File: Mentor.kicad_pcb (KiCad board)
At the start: 2 copper layers, 50 x 100 mm, 41 parts, among them J1 CONN_01X02, J2 CONN_01X06, J3 CONN_01X09, J4 CONN_01X10, J5 CONN_01X02, J6 CONN_01X03, J7 CONN_01X09, Q1 PZT2222A, Q2 PZT2222A, Q3 IRFR3303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

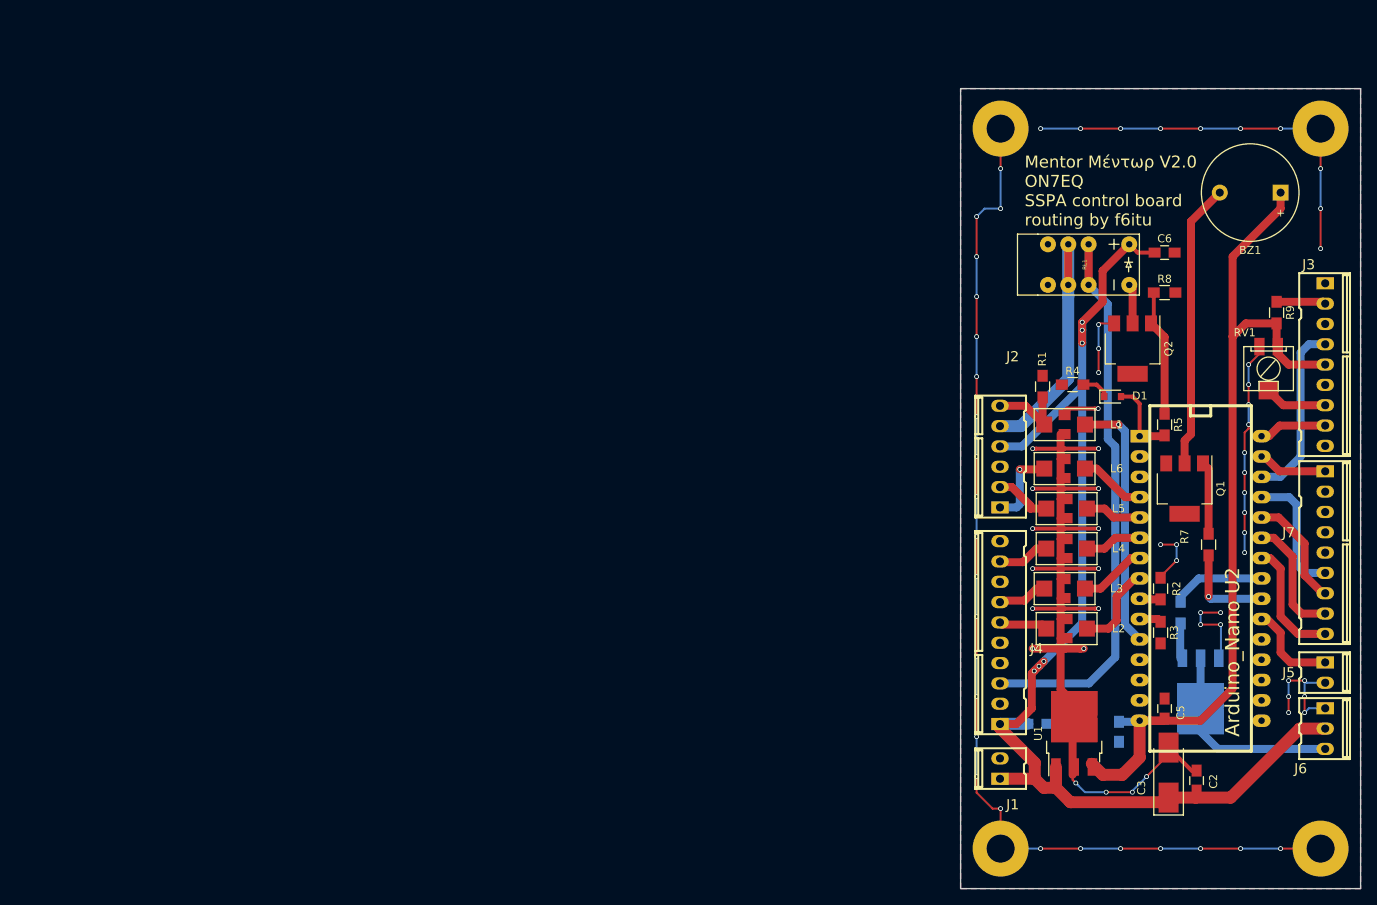
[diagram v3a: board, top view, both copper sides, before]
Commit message: Mentor V3.0 W6PQL compatible
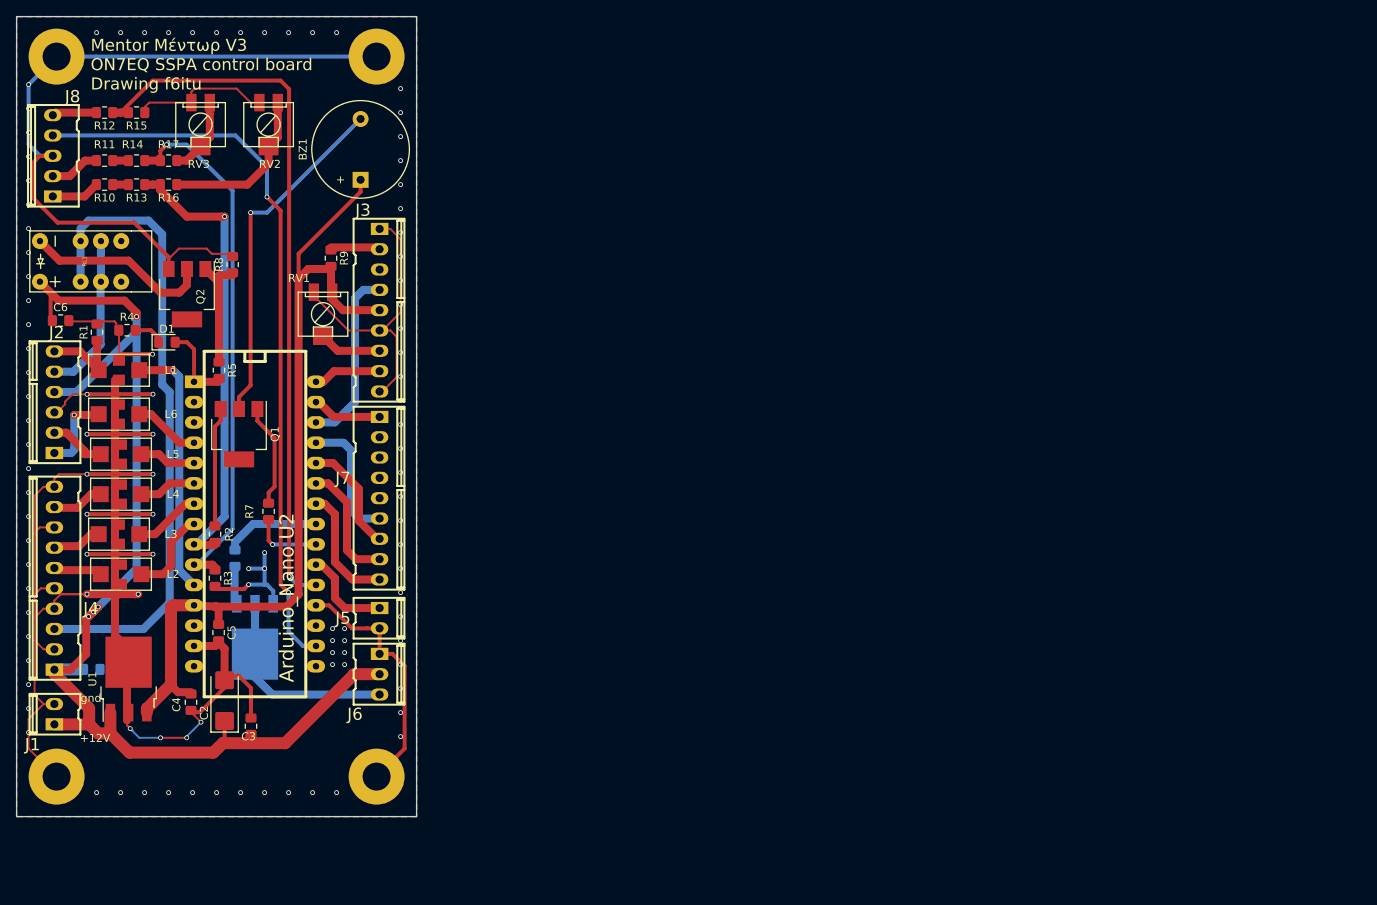
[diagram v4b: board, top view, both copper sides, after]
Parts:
- added J8: Conn_01x05, conn_kk100:kk100_22-23-2051, F.Cu at (46.6, 43.4)
- added R10: 5k, Resistor_SMD:R_0805_2012Metric_Pad1.15x1.40mm_HandSolder, F.Cu at (53.0, 47.0)
- added R11: 1k5, Resistor_SMD:R_0805_2012Metric_Pad1.15x1.40mm_HandSolder, F.Cu at (53.0, 44.0)
- added R12: 3k3, Resistor_SMD:R_0805_2012Metric_Pad1.15x1.40mm_HandSolder, F.Cu at (53.0, 38.0)
- added R13: 2k, Resistor_SMD:R_0805_2012Metric_Pad1.15x1.40mm_HandSolder, F.Cu at (57.0, 47.0)
- added R14: 1k5, Resistor_SMD:R_0805_2012Metric_Pad1.15x1.40mm_HandSolder, F.Cu at (57.0, 44.0)
- added R15: 1k5, Resistor_SMD:R_0805_2012Metric_Pad1.15x1.40mm_HandSolder, F.Cu at (57.0, 38.0)
- added R16: 500R, Resistor_SMD:R_0805_2012Metric_Pad1.15x1.40mm_HandSolder, F.Cu at (61.0, 47.0)
- added R17: 500R, Resistor_SMD:R_0805_2012Metric_Pad1.15x1.40mm_HandSolder, F.Cu at (61.0, 44.0)
- added RV2: 2k, Trimmer_3314G1_Handsoldering:Trimmer_3314G1_Handsoldering, F.Cu at (73.5, 39.5)
- added RV3: 2k, Trimmer_3314G1_Handsoldering:Trimmer_3314G1_Handsoldering, F.Cu at (65.0, 39.5)
- BZ1: footprint Buzzers_Beepers:Buzzer_12x9.5RM7.6 -> Buzzer_Beeper:Buzzer_12x9.5RM7.6
- C1, C3, C5, C6: footprint Capacitors_SMD:C_0805_HandSoldering -> Capacitor_SMD:C_0805_2012Metric_Pad1.15x1.40mm_HandSolder
- C2: footprint Capacitors_Tantalum_SMD:CP_Tantalum_Case-C_EIA-6032-28_Hand -> Capacitor_Tantalum_SMD:CP_EIA-6032-28_Kemet-C_Pad2.25x2.35mm_HandSolder
- C4: footprint Capacitors_SMD:C_0805_HandSoldering -> Capacitor_SMD:C_0805_2012Metric_Pad1.15x1.40mm_HandSolder; moved to F.Cu
- D1: footprint Diodes_SMD:D_0805 -> Diode_SMD:D_0805_2012Metric_Pad1.15x1.40mm_HandSolder
- Q1, Q2: footprint TO_SOT_Packages_SMD:SOT-223 -> Package_TO_SOT_SMD:SOT-223
- Q3, U1: footprint TO_SOT_Packages_SMD:TO-252-3_TabPin2 -> Package_TO_SOT_SMD:TO-252-3_TabPin2
- R1, R2, R3, R4, R5, R6, R7, R8, R9: footprint Resistors_SMD:R_0805_HandSoldering -> Resistor_SMD:R_0805_2012Metric_Pad1.15x1.40mm_HandSolder
- moved C6 138.3 mm to (47.5, 64.0)
- moved RL1 126.0 mm to (50.0, 56.6), turned to 90 degrees
- moved C5 118.6 mm to (67.2, 103.0), turned to 270 degrees
- moved C3 118.4 mm to (71.3, 114.7)
- moved D1 118.4 mm to (60.8, 66.7)
- moved J1 118.4 mm to (46.8, 113.2)
- moved J2 118.4 mm to (46.8, 74.2)
- moved J3 118.4 mm to (87.3, 62.7)
- moved J4 118.4 mm to (46.8, 96.2)
- moved J5 118.4 mm to (87.3, 101.2)
- moved J6 118.4 mm to (87.3, 108.2)
- moved J7 118.4 mm to (87.3, 86.2)
- moved L1 118.4 mm to (54.8, 70.2)
- moved L2 118.4 mm to (55.0, 95.7)
- moved L3 118.4 mm to (54.8, 90.7)
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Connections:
- J3 pad 3: (no net) -> Net-(J3-Pad3)
- J7 pad 2: (no net) -> Net-(J7-Pad2)
- J7 pad 3: (no net) -> Net-(J7-Pad3)
- J7 pad 4: (no net) -> Net-(J7-Pad4)
- J7 pad 5: (no net) -> Net-(J7-Pad5)
- RL1 pad 5: (no net) -> Net-(RL1-Pad5)
- RL1 pad 8: (no net) -> Net-(RL1-Pad8)
- U2 pad 12: (no net) -> +5V
- U2 pad 13: (no net) -> Net-(U2-Pad13)
- U2 pad 15: +5V -> Net-(U2-Pad15)
- U2 pad 16: (no net) -> Net-(U2-Pad16)
- U2 pad 17: (no net) -> Net-(J8-Pad4)
- U2 pad 18: (no net) -> Net-(U2-Pad18)
- U2 pad 2: (no net) -> Net-(U2-Pad2)
- U2 pad 20: (no net) -> Net-(R12-Pad1)
- U2 pad 3: (no net) -> Net-(U2-Pad3)
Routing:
- net Net-(J8-Pad4): track 0.00 -> 91.8 mm, vias 0 -> 2
- net Net-(R12-Pad1): track 0.00 -> 89.8 mm, vias 0 -> 1
- net Net-(R14-Pad1): track 2.76 -> 66.6 mm, vias 0 -> 1
- net GND: track 371.5 -> 430.2 mm, vias 79 -> 107
- net Net-(R13-Pad1): track 2.65 -> 57.5 mm, vias 0 -> 1
- net Net-(R16-Pad1): track 0.00 -> 20.6 mm
- net Net-(Q2-Pad2): track 4.98 -> 23.4 mm
- net Net-(J2-Pad5): track 33.4 -> 20.1 mm
- net Net-(R17-Pad1): track 0.00 -> 9.68 mm
- net Net-(BZ1-Pad2): track 35.7 -> 43.7 mm, vias 0 -> 1
- net +5V: track 113.0 -> 106.4 mm
- net Net-(J4-Pad3): track 73.8 -> 80.2 mm
- net Net-(J8-Pad2): track 0.00 -> 6.25 mm
- net Net-(J8-Pad1): track 0.00 -> 6.06 mm
- net Net-(J8-Pad5): track 0.00 -> 5.58 mm
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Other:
- board text added: "+12V"
- board text added: "By-pass/Operate Reset/Alarm GND 12V Sense 24V Sense"
- board text added: "From U Amp"
- board text added: "Mentor Μέντωρ V3 ON7EQ SSPA control board Drawing f6itu"
- board text added: "To 4x40 Display"
- board text added: "To Fan"
- board text added: "To Telemaque"
- board text added: "gnd"
- board text removed: "Mentor Μέντωρ V2.0 ON7EQ SSPA control board routing by f6itu"

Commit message: new schematic for w6pql compatibility
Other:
- net class Default removed
